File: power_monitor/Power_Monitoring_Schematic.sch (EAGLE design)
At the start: 14 parts, among them U1 INA3221.

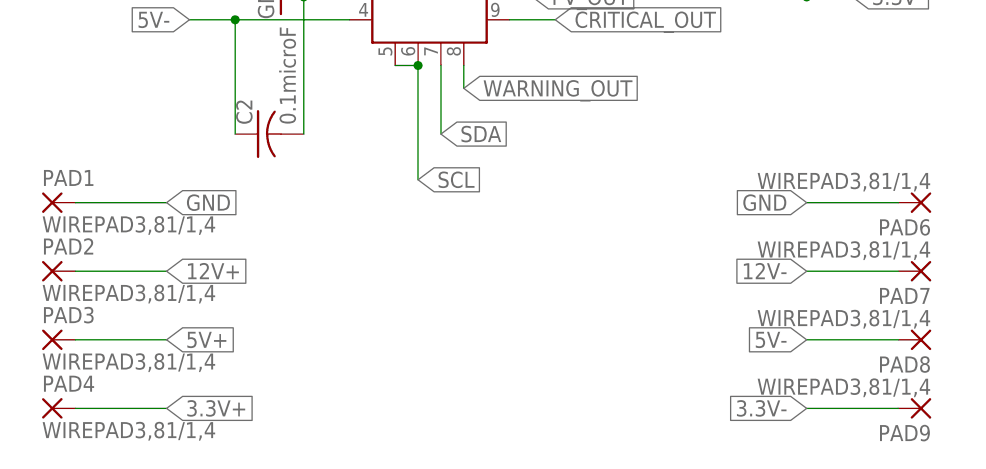
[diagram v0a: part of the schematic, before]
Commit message: Changed routings
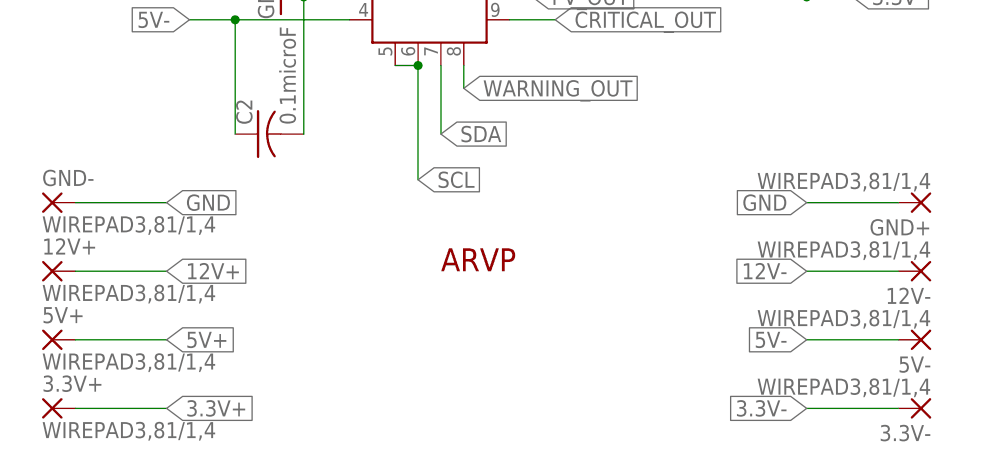
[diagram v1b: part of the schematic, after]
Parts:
- added ARVP1: ARVP_LOGO, ARVP:ARVP_LOGO
- renumbered PAD1 to GND-, PAD2 to 12V+, PAD3 to 5V+, PAD4 to 3.3V+, PAD6 to GND+, PAD7 to 12V-, PAD8 to 5V-, PAD9 to 3.3V-
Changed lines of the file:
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@@
 <part name="I2C" library="pinhead" library_urn="urn:adsk.eagle:library:325" deviceset="PINHD-1X4" device="" package3d_urn="urn:adsk.eagle:package:22407/2"/>
 <part name="GND1" library="supply1" deviceset="GND" device=""/>
-<part name="PAD1" library="wirepad" library_urn="urn:adsk.eagle:library:412" deviceset="WIREPAD" device="3,81/1,4" package3d_urn="urn:adsk.eagle:package:30835/1"/>
-<part name="PAD2" library="wirepad" library_urn="urn:adsk.eagle:library:412" deviceset="WIREPAD" device="3,81/1,4" package3d_urn="urn:adsk.eagle:package:30835/1"/>
-<part name="PAD3" library="wirepad" library_urn="urn:adsk.eagle:library:412" deviceset="WIREPAD" device="3,81/1,4" package3d_urn="urn:adsk.eagle:package:30835/1"/>
-<part name="PAD4" library="wirepad" library_urn="urn:adsk.eagle:library:412" deviceset="WIREPAD" device="3,81/1,4" package3d_urn="urn:adsk.eagle:package:30835/1"/>
-<part name="PAD6" library="wirepad" library_urn="urn:adsk.eagle:library:412" deviceset="WIREPAD" device="3,81/1,4" package3d_urn="urn:adsk.eagle:package:30835/1"/>
-<part name="PAD7" library="wirepad" library_urn="urn:adsk.eagle:library:412" deviceset="WIREPAD" device="3,81/1,4" package3d_urn="urn:adsk.eagle:package:30835/1"/>
-<part name="PAD8" library="wirepad" library_urn="urn:adsk.eagle:library:412" deviceset="WIREPAD" device="3,81/1,4" package3d_urn="urn:adsk.eagle:package:30835/1"/>
-<part name="PAD9" library="wirepad" library_urn="urn:adsk.eagle:library:412" deviceset="WIREPAD" device="3,81/1,4" package3d_urn="urn:adsk.eagle:package:30835/1"/>
+<part name="GND-" library="wirepad" library_urn="urn:adsk.eagle:library:412" deviceset="WIREPAD" device="3,81/1,4" package3d_urn="urn:adsk.eagle:package:30835/1"/>
+<part name="12V+" library="wirepad" library_urn="urn:adsk.eagle:library:412" deviceset="WIREPAD" device="3,81/1,4" package3d_urn="urn:adsk.eagle:package:30835/1"/>
+<part name="5V+" library="wirepad" library_urn="urn:adsk.eagle:library:412" deviceset="WIREPAD" device="3,81/1,4" package3d_urn="urn:adsk.eagle:package:30835/1"/>
+<part name="3.3V+" library="wirepad" library_urn="urn:adsk.eagle:library:412" deviceset="WIREPAD" device="3,81/1,4" package3d_urn="urn:adsk.eagle:package:30835/1"/>
+<part name="GND+" library="wirepad" library_urn="urn:adsk.eagle:library:412" deviceset="WIREPAD" device="3,81/1,4" package3d_urn="urn:adsk.eagle:package:30835/1"/>
+<part name="12V-" library="wirepad" library_urn="urn:adsk.eagle:library:412" deviceset="WIREPAD" device="3,81/1,4" package3d_urn="urn:adsk.eagle:package:30835/1"/>
+<part name="5V-" library="wirepad" library_urn="urn:adsk.eagle:library:412" deviceset="WIREPAD" device="3,81/1,4" package3d_urn="urn:adsk.eagle:package:30835/1"/>
+<part name="3.3V-" library="wirepad" library_urn="urn:adsk.eagle:library:412" deviceset="WIREPAD" device="3,81/1,4" package3d_urn="urn:adsk.eagle:package:30835/1"/>
+<part name="ARVP1" library="ARVP" deviceset="ARVP_LOGO" device=""/>
 </parts>
 <sheets>
@@
 <instance part="I2C" gate="A" x="-20.32" y="30.48"/>
 <instance part="GND1" gate="1" x="-35.56" y="25.4"/>
-<instance part="PAD1" gate="G$1" x="-43.18" y="-22.86"/>
-<instance part="PAD2" gate="G$1" x="-43.18" y="-30.48"/>
-<instance part="PAD3" gate="G$1" x="-43.18" y="-38.1"/>
-<instance part="PAD4" gate="G$1" x="-43.18" y="-45.72"/>
-<instance part="PAD6" gate="G$1" x="53.34" y="-22.86" rot="R180"/>
-<instance part="PAD7" gate="G$1" x="53.34" y="-30.48" rot="R180"/>
-<instance part="PAD8" gate="G$1" x="53.34" y="-38.1" rot="R180"/>
-<instance part="PAD9" gate="G$1" x="53.34" y="-45.72" rot="R180"/>
+<instance part="GND-" gate="G$1" x="-43.18" y="-22.86"/>
+<instance part="12V+" gate="G$1" x="-43.18" y="-30.48"/>
+<instance part="5V+" gate="G$1" x="-43.18" y="-38.1"/>
+<instance part="3.3V+" gate="G$1" x="-43.18" y="-45.72"/>
+<instance part="GND+" gate="G$1" x="53.34" y="-22.86" rot="R180"/>
+<instance part="12V-" gate="G$1" x="53.34" y="-30.48" rot="R180"/>
+<instance part="5V-" gate="G$1" x="53.34" y="-38.1" rot="R180"/>
+<instance part="3.3V-" gate="G$1" x="53.34" y="-45.72" rot="R180"/>
+<instance part="ARVP1" gate="G$1" x="2.54" y="-30.48"/>
 </instances>
 <busses>
@@
 </segment>
 <segment>
-<pinref part="PAD1" gate="G$1" pin="P"/>
+<pinref part="GND-" gate="G$1" pin="P"/>
 <wire x1="-40.64" y1="-22.86" x2="-30.48" y2="-22.86" width="0.1524" layer="91"/>
 <label x="-30.48" y="-22.86" size="1.778" layer="95" xref="yes"/>
 </segment>
 <segment>
-<pinref part="PAD6" gate="G$1" pin="P"/>
+<pinref part="GND+" gate="G$1" pin="P"/>
 <wire x1="50.8" y1="-22.86" x2="40.64" y2="-22.86" width="0.1524" layer="91"/>
 <label x="40.64" y="-22.86" size="1.778" layer="95" rot="R180" xref="yes"/>
@@
 </segment>
 <segment>
-<pinref part="PAD4" gate="G$1" pin="P"/>
+<pinref part="3.3V+" gate="G$1" pin="P"/>
 <wire x1="-40.64" y1="-45.72" x2="-30.48" y2="-45.72" width="0.1524" layer="91"/>
 <label x="-30.48" y="-45.72" size="1.778" layer="95" xref="yes"/>
@@
 </segment>
 <segment>
-<pinref part="PAD3" gate="G$1" pin="P"/>
+<pinref part="5V+" gate="G$1" pin="P"/>
 <wire x1="-40.64" y1="-38.1" x2="-30.48" y2="-38.1" width="0.1524" layer="91"/>
 <label x="-30.48" y="-38.1" size="1.778" layer="95" xref="yes"/>
@@
 </segment>
 <segment>
-<pinref part="PAD9" gate="G$1" pin="P"/>
+<pinref part="3.3V-" gate="G$1" pin="P"/>
 <wire x1="50.8" y1="-45.72" x2="40.64" y2="-45.72" width="0.1524" layer="91"/>
 <label x="40.64" y="-45.72" size="1.778" layer="95" rot="R180" xref="yes"/>
@@
 </segment>
 <segment>
-<pinref part="PAD8" gate="G$1" pin="P"/>
+<pinref part="5V-" gate="G$1" pin="P"/>
 <wire x1="50.8" y1="-38.1" x2="40.64" y2="-38.1" width="0.1524" layer="91"/>
 <label x="40.64" y="-38.1" size="1.778" layer="95" rot="R180" xref="yes"/>
@@
 </segment>
 <segment>
-<pinref part="PAD2" gate="G$1" pin="P"/>
+<pinref part="12V+" gate="G$1" pin="P"/>
 <wire x1="-40.64" y1="-30.48" x2="-30.48" y2="-30.48" width="0.1524" layer="91"/>
 <label x="-30.48" y="-30.48" size="1.778" layer="95" xref="yes"/>
@@
 </segment>
 <segment>
-<pinref part="PAD7" gate="G$1" pin="P"/>
+<pinref part="12V-" gate="G$1" pin="P"/>
 <wire x1="50.8" y1="-30.48" x2="40.64" y2="-30.48" width="0.1524" layer="91"/>
 <label x="40.64" y="-30.48" size="1.778" layer="95" rot="R180" xref="yes"/>

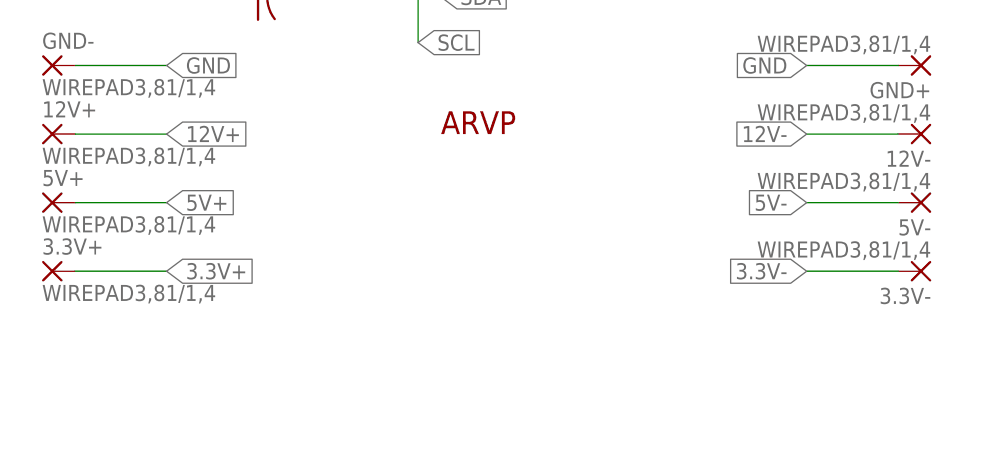
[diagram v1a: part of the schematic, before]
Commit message: Added and move GND wire pads and added a top and bootom GND plane
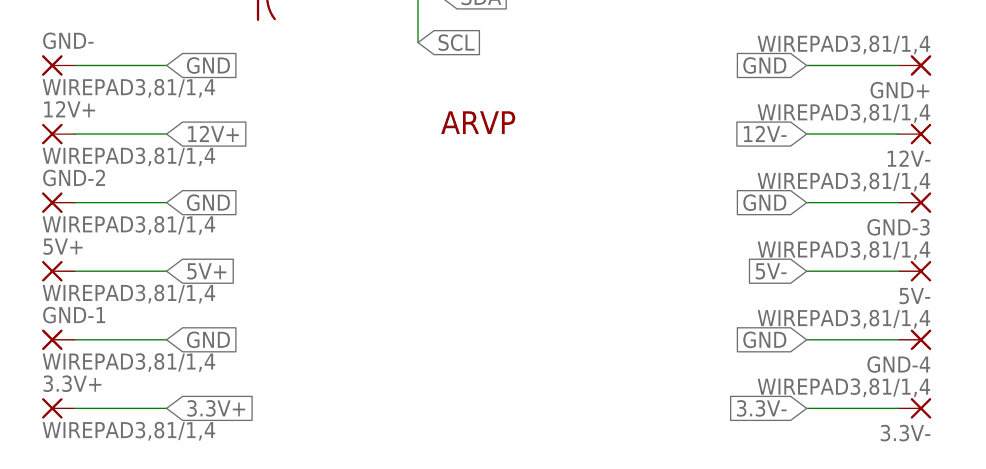
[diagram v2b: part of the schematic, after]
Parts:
- added GND-1, GND-2, GND-3, GND-4: WIREPAD3,81/1,4, wirepad:WIREPAD3,81/1,4
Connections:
- net GND: now also GND-1.P, GND-2.P, GND-3.P, GND-4.P
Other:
- moved on the sheet: 3.3V+, 3.3V-, 5V+, 5V-
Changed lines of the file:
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@@
 <part name="3.3V-" library="wirepad" library_urn="urn:adsk.eagle:library:412" deviceset="WIREPAD" device="3,81/1,4" package3d_urn="urn:adsk.eagle:package:30835/1"/>
 <part name="ARVP1" library="ARVP" deviceset="ARVP_LOGO" device=""/>
+<part name="GND-1" library="wirepad" library_urn="urn:adsk.eagle:library:412" deviceset="WIREPAD" device="3,81/1,4" package3d_urn="urn:adsk.eagle:package:30835/1"/>
+<part name="GND-2" library="wirepad" library_urn="urn:adsk.eagle:library:412" deviceset="WIREPAD" device="3,81/1,4" package3d_urn="urn:adsk.eagle:package:30835/1"/>
+<part name="GND-3" library="wirepad" library_urn="urn:adsk.eagle:library:412" deviceset="WIREPAD" device="3,81/1,4" package3d_urn="urn:adsk.eagle:package:30835/1"/>
+<part name="GND-4" library="wirepad" library_urn="urn:adsk.eagle:library:412" deviceset="WIREPAD" device="3,81/1,4" package3d_urn="urn:adsk.eagle:package:30835/1"/>
 </parts>
 <sheets>
@@
 <instance part="GND-" gate="G$1" x="-43.18" y="-22.86"/>
 <instance part="12V+" gate="G$1" x="-43.18" y="-30.48"/>
-<instance part="5V+" gate="G$1" x="-43.18" y="-38.1"/>
-<instance part="3.3V+" gate="G$1" x="-43.18" y="-45.72"/>
+<instance part="5V+" gate="G$1" x="-43.18" y="-45.72"/>
+<instance part="3.3V+" gate="G$1" x="-43.18" y="-60.96"/>
 <instance part="GND+" gate="G$1" x="53.34" y="-22.86" rot="R180"/>
 <instance part="12V-" gate="G$1" x="53.34" y="-30.48" rot="R180"/>
-<instance part="5V-" gate="G$1" x="53.34" y="-38.1" rot="R180"/>
-<instance part="3.3V-" gate="G$1" x="53.34" y="-45.72" rot="R180"/>
+<instance part="5V-" gate="G$1" x="53.34" y="-45.72" rot="R180"/>
+<instance part="3.3V-" gate="G$1" x="53.34" y="-60.96" rot="R180"/>
 <instance part="ARVP1" gate="G$1" x="2.54" y="-30.48"/>
+<instance part="GND-1" gate="G$1" x="-43.18" y="-53.34"/>
+<instance part="GND-2" gate="G$1" x="-43.18" y="-38.1"/>
+<instance part="GND-3" gate="G$1" x="53.34" y="-38.1" rot="R180"/>
+<instance part="GND-4" gate="G$1" x="53.34" y="-53.34" rot="R180"/>
 </instances>
 <busses>
@@
 <label x="40.64" y="-22.86" size="1.778" layer="95" rot="R180" xref="yes"/>
 </segment>
+<segment>
+<pinref part="GND-1" gate="G$1" pin="P"/>
+<wire x1="-40.64" y1="-53.34" x2="-30.48" y2="-53.34" width="0.1524" layer="91"/>
+<label x="-30.48" y="-53.34" size="1.778" layer="95" xref="yes"/>
+</segment>
+<segment>
+<pinref part="GND-2" gate="G$1" pin="P"/>
+<wire x1="-40.64" y1="-38.1" x2="-30.48" y2="-38.1" width="0.1524" layer="91"/>
+<label x="-30.48" y="-38.1" size="1.778" layer="95" xref="yes"/>
+</segment>
+<segment>
+<pinref part="GND-3" gate="G$1" pin="P"/>
+<wire x1="50.8" y1="-38.1" x2="40.64" y2="-38.1" width="0.1524" layer="91"/>
+<label x="40.64" y="-38.1" size="1.778" layer="95" rot="R180" xref="yes"/>
+</segment>
+<segment>
+<pinref part="GND-4" gate="G$1" pin="P"/>
+<wire x1="50.8" y1="-53.34" x2="40.64" y2="-53.34" width="0.1524" layer="91"/>
+<label x="40.64" y="-53.34" size="1.778" layer="95" rot="R180" xref="yes"/>
+</segment>
 </net>
 <net name="3.3V+" class="0">
@@
 <segment>
 <pinref part="3.3V+" gate="G$1" pin="P"/>
-<wire x1="-40.64" y1="-45.72" x2="-30.48" y2="-45.72" width="0.1524" layer="91"/>
-<label x="-30.48" y="-45.72" size="1.778" layer="95" xref="yes"/>
+<wire x1="-40.64" y1="-60.96" x2="-30.48" y2="-60.96" width="0.1524" layer="91"/>
+<label x="-30.48" y="-60.96" size="1.778" layer="95" xref="yes"/>
 </segment>
 </net>
@@
 <segment>
 <pinref part="5V+" gate="G$1" pin="P"/>
-<wire x1="-40.64" y1="-38.1" x2="-30.48" y2="-38.1" width="0.1524" layer="91"/>
-<label x="-30.48" y="-38.1" size="1.778" layer="95" xref="yes"/>
+<wire x1="-40.64" y1="-45.72" x2="-30.48" y2="-45.72" width="0.1524" layer="91"/>
+<label x="-30.48" y="-45.72" size="1.778" layer="95" xref="yes"/>
 </segment>
 </net>
@@
 <segment>
 <pinref part="3.3V-" gate="G$1" pin="P"/>
-<wire x1="50.8" y1="-45.72" x2="40.64" y2="-45.72" width="0.1524" layer="91"/>
-<label x="40.64" y="-45.72" size="1.778" layer="95" rot="R180" xref="yes"/>
+<wire x1="50.8" y1="-60.96" x2="40.64" y2="-60.96" width="0.1524" layer="91"/>
+<label x="40.64" y="-60.96" size="1.778" layer="95" rot="R180" xref="yes"/>
 </segment>
 </net>
@@
 <segment>
 <pinref part="5V-" gate="G$1" pin="P"/>
-<wire x1="50.8" y1="-38.1" x2="40.64" y2="-38.1" width="0.1524" layer="91"/>
-<label x="40.64" y="-38.1" size="1.778" layer="95" rot="R180" xref="yes"/>
+<wire x1="50.8" y1="-45.72" x2="40.64" y2="-45.72" width="0.1524" layer="91"/>
+<label x="40.64" y="-45.72" size="1.778" layer="95" rot="R180" xref="yes"/>
 </segment>
 <segment>

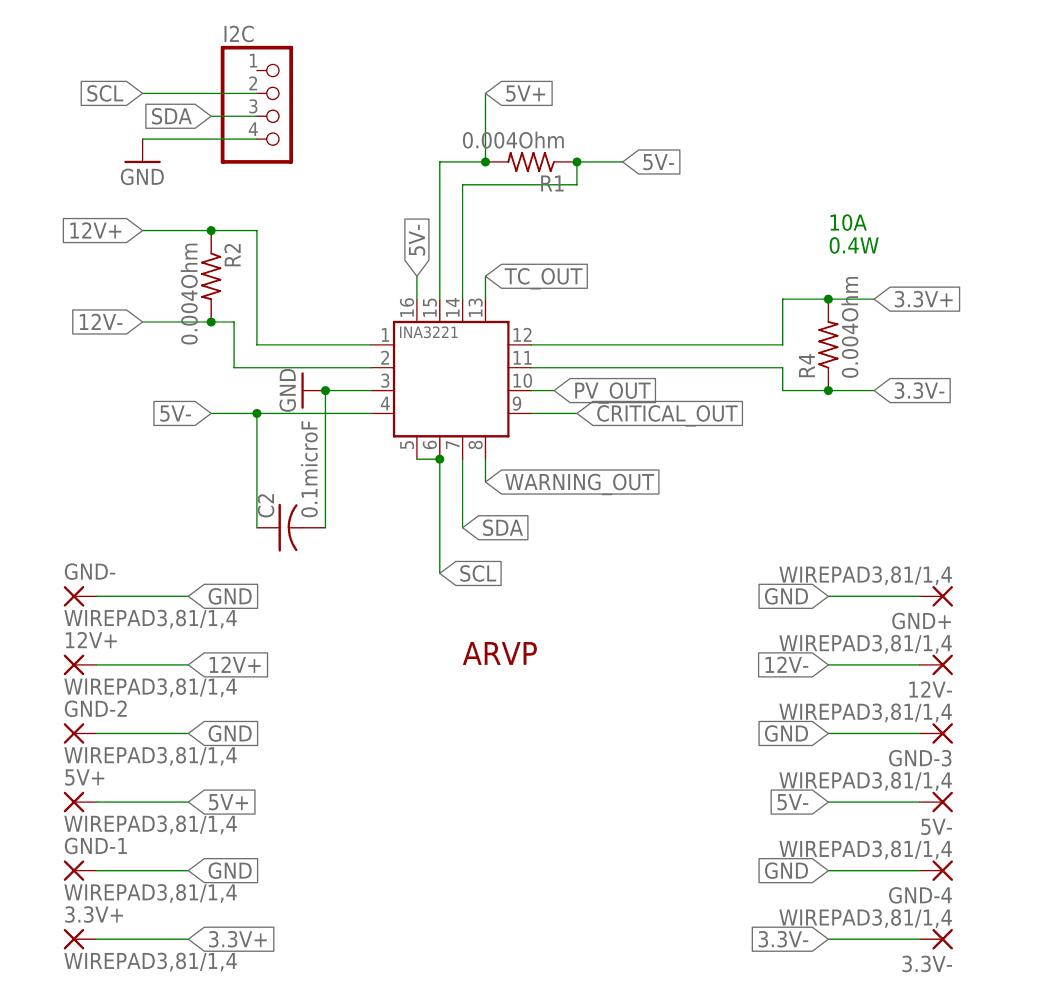
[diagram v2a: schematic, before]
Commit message: Removed extra GND pads, increased drill size to 1.5mm'
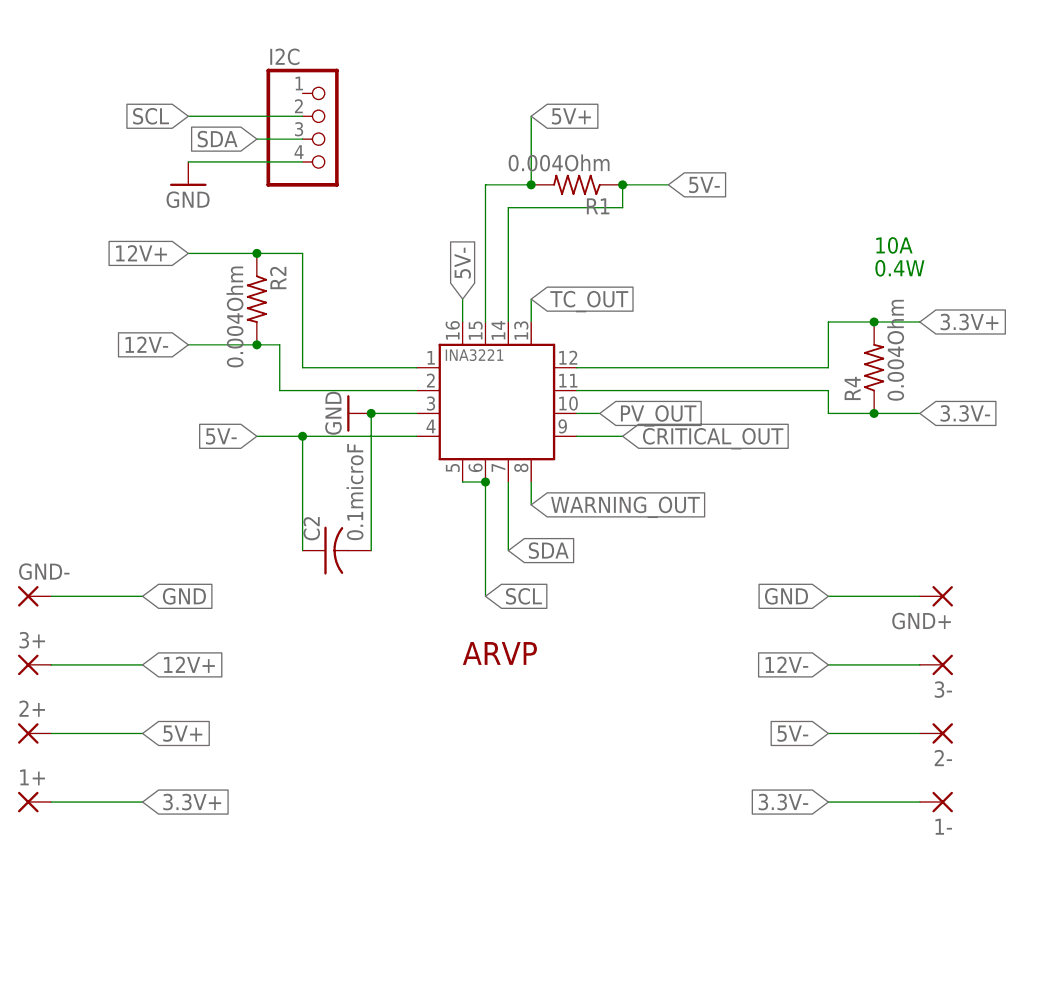
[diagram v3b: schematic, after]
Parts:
- removed 12V+, 12V-, 3.3V+, 3.3V-, 5V+, 5V-, GND-1, GND-2, GND-3, GND-4: WIREPAD3,81/1,4, wirepad:WIREPAD3,81/1,4
- added 1+, 1-, 2+, 2-, 3+, 3-: (no value), Moira:3,81/1,5A
- GND+, GND-: value WIREPAD3,81/1,4 -> (none); device wirepad:WIREPAD3,81/1,4 -> Moira:3,81/1,5A
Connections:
- net 12V+: now also 3+.P; no longer 12V+.P
- net 12V-: now also 3-.P; no longer 12V-.P
- net 3.3V+: now also 1+.P; no longer 3.3V+.P
- net 3.3V-: now also 1-.P; no longer 3.3V-.P
- net 5V+: now also 2+.P; no longer 5V+.P
- net 5V-: now also 2-.P; no longer 5V-.P
- net GND: no longer GND-1.P, GND-2.P, GND-3.P, GND-4.P
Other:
- moved on the sheet: C2, I2C, R1, R2, R4
